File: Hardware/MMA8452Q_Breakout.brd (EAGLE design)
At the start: 15.2 x 15.2 mm, 16 parts, among them U1 MMA8452QMMA8452Q-1:1

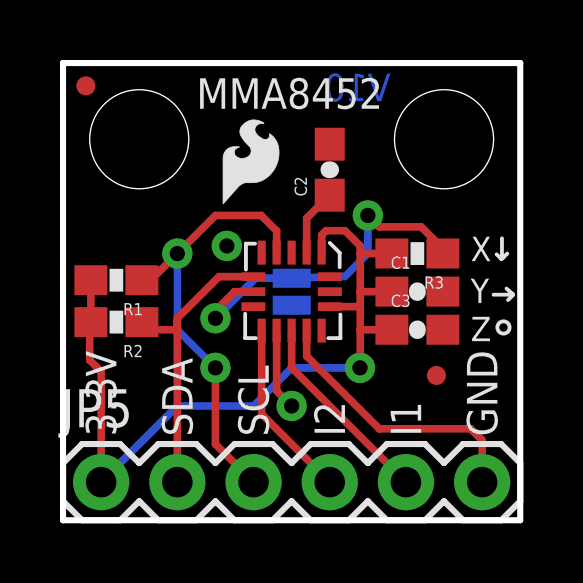
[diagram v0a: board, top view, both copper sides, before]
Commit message: added board fiducials
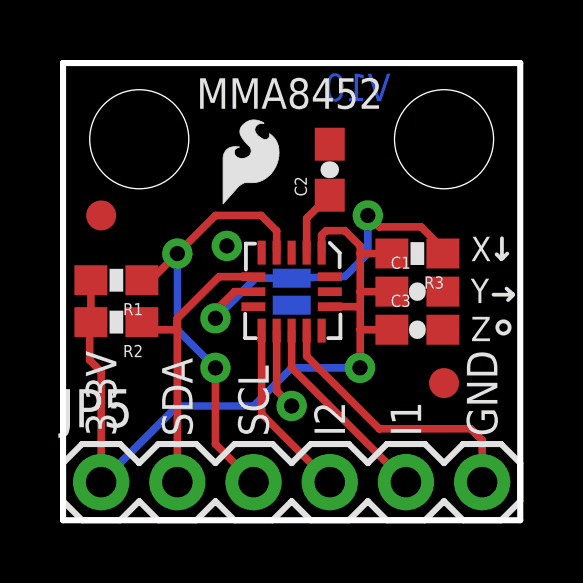
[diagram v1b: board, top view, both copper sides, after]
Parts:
- removed JP2, JP6: FIDUCIALUFIDUCIAL, SparkFun:MICRO-FIDUCIAL
- added FID1, FID2: FIDUCIAL1X2, SparkFun-Aesthetics:FIDUCIAL-1X2
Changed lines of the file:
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@@
 <?xml version="1.0" encoding="utf-8"?>
 <!DOCTYPE eagle SYSTEM "eagle.dtd">
-<eagle version="6.4">
+<eagle version="6.5.0">
 <drawing>
 <settings>
@@
 <setting verticaltext="up"/>
 </settings>
-<grid distance="0.05" unitdist="inch" unit="inch" style="lines" multiple="1" display="yes" altdistance="0.005" altunitdist="inch" altunit="inch"/>
+<grid distance="0.05" unitdist="inch" unit="inch" style="lines" multiple="1" display="yes" altdistance="0.01" altunitdist="inch" altunit="inch"/>
 <layers>
 <layer number="1" name="Top" color="4" fill="1" visible="yes" active="yes"/>
@@
 <layer number="18" name="Vias" color="2" fill="1" visible="yes" active="yes"/>
 <layer number="19" name="Unrouted" color="6" fill="1" visible="yes" active="yes"/>
-<layer number="20" name="Dimension" color="15" fill="1" visible="yes" active="yes"/>
-<layer number="21" name="tPlace" color="16" fill="1" visible="yes" active="yes"/>
-<layer number="22" name="bPlace" color="14" fill="1" visible="yes" active="yes"/>
+<layer number="20" name="Dimension" color="6" fill="1" visible="yes" active="yes"/>
+<layer number="21" name="tPlace" color="6" fill="1" visible="yes" active="yes"/>
+<layer number="22" name="bPlace" color="6" fill="1" visible="yes" active="yes"/>
 <layer number="23" name="tOrigins" color="15" fill="1" visible="yes" active="yes"/>
 <layer number="24" name="bOrigins" color="15" fill="1" visible="yes" active="yes"/>
@@
 <element name="JP5" library="SparkFun" package="1X06" value="" x="1.27" y="1.27"/>
 <element name="SJ1" library="SparkFun" package="SJ_2S-NO" value="" x="7.62" y="7.62" rot="MR90"/>
-<element name="JP2" library="SparkFun" package="MICRO-FIDUCIAL" value="FIDUCIALUFIDUCIAL" x="12.446" y="4.826"/>
-<element name="JP6" library="SparkFun" package="MICRO-FIDUCIAL" value="FIDUCIALUFIDUCIAL" x="0.762" y="14.478"/>
 <element name="FRAME1" library="SparkFun-Aesthetics" package="CREATIVE_COMMONS" value="FRAME-LETTER" x="-123.932121875" y="0"/>
+<element name="FID1" library="SparkFun-Aesthetics" package="FIDUCIAL-1X2" value="FIDUCIAL1X2" x="1.27" y="10.16"/>
+<element name="FID2" library="SparkFun-Aesthetics" package="FIDUCIAL-1X2" value="FIDUCIAL1X2" x="12.7" y="4.572"/>
 </elements>
 <signals>
